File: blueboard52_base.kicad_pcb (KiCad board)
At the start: 2 copper layers, 42.4 x 43.1 mm, 16 parts, among them J1 Conn_East, J2 Conn_West, J3 Conn_South, J4 Conn_VCC, J5 Conn_GND, J6 PBAT, J7 PEXT, SW1 RST, SW2 DFU, U1 E73-2G4M04S-52832

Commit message: Added version info to the board
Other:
- board text added: "v0.1.1, git.io/JegEw"
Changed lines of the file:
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@@
   (general
     (thickness 1.6)
-    (drawings 37)
+    (drawings 38)
     (tracks 172)
     (zones 0)
@@
       (xy -2.020742 1.935137) (xy -2.615037 2.435648) (xy -2.618079 2.434865)) (layer F.SilkS) (width 0))
   )
+  (gr_text "v0.1.1, git.io/JegEw" (at 120.1 89.5) (layer B.SilkS)
+    (effects (font (size 1.5 1.5) (thickness 0.3)) (justify left mirror))
+  )
   (gr_text 15 (at 115.076014 85.275774 270) (layer B.SilkS)

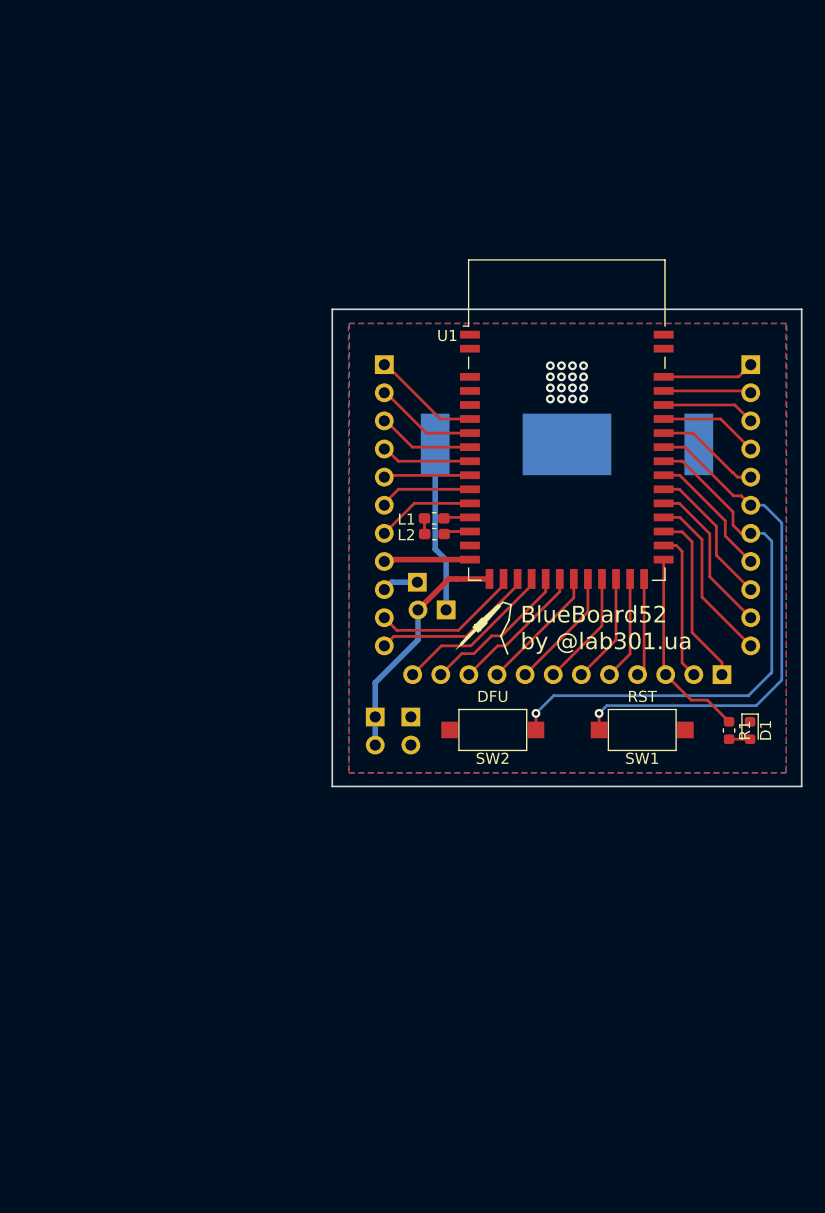
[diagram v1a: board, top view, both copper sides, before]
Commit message: New version of the board - v0.2.0
- Added a separate NFC header
- Created a solid (almost) ground plane on the bottom
- Added silkscreen markings to the top layer
- Removed a bulky power source selector - either a BAT jumper or
  external power source can now be used to power the board
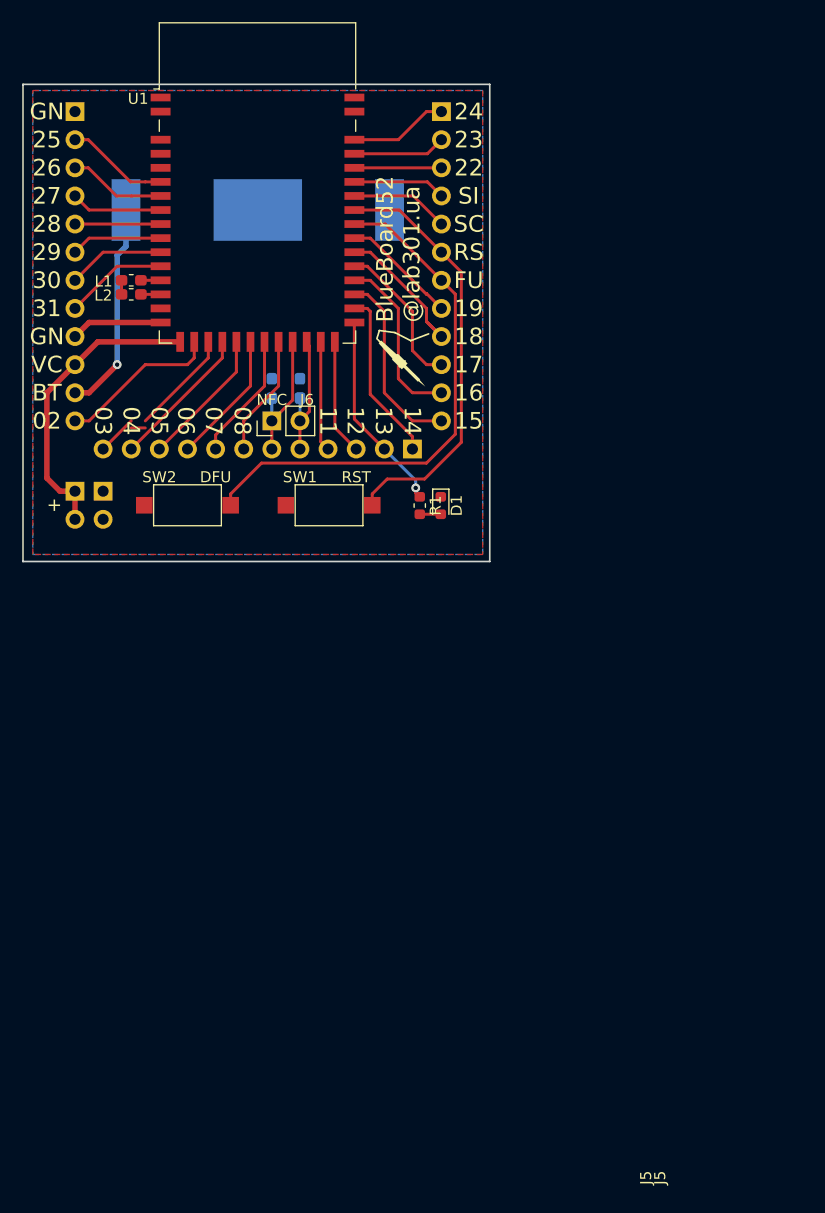
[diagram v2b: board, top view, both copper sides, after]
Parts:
- removed J7: PEXT, Connector_PinHeader_2.54mm:PinHeader_1x01_P2.54mm_Vertical
- added ?: , , F.Cu at (55.4, 62.0)
- added ?: , , F.Cu at (54.1, 62.0)
- added C1: 300pf, Capacitor_SMD:C_0603_1608Metric_Pad1.05x0.95mm_HandSolder, B.Cu at (77.0, 56.5)
- added C2: 300pf, Capacitor_SMD:C_0603_1608Metric_Pad1.05x0.95mm_HandSolder, B.Cu at (74.4, 56.5)
- J1, J2: footprint Connector_PinHeader_2.54mm:PinHeader_1x11_P2.54mm_Vertical -> Connector_PinHeader_2.54mm:PinHeader_1x12_P2.54mm_Vertical
- J4: value Conn_VCC -> VCC
- J5: value Conn_GND -> GND
- J6: value PBAT -> NFC; moved to F.Cu
- moved J1 36.1 mm to (89.8, 31.5)
- moved J2 36.1 mm to (56.7, 31.5)
- moved U1 35.2 mm to (73.1, 38.0)
- moved BT1 35.0 mm to (73.2, 40.4)
- moved L2 34.9 mm to (61.7, 48.0)
- moved SW1 34.8 mm to (79.6, 67.1), turned to 0 degrees
- moved L1 34.8 mm to (61.7, 46.8)
- moved J3 34.6 mm to (87.1, 62.0)
- moved D1 34.5 mm to (89.7, 67.1)
- moved R1 34.5 mm to (87.8, 67.1)
- moved J5 34.5 mm to (59.2, 65.8)
- moved SW2 34.2 mm to (66.8, 67.1)
- moved J4 33.9 mm to (56.7, 65.8)
- moved svg2mod 25.2 mm to (85.9, 53.8), turned to 90 degrees
- moved J6 23.2 mm to (74.4, 59.5)
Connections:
- J2 pad 1: /P0.25 -> GND
- J2 pad 10: /P0.2 -> VCC
- J2 pad 11: /P0.3 -> +BATT
- J2 pad 2: /P0.26 -> /P0.25
- J2 pad 3: /P0.27 -> /P0.26
- J2 pad 4: /P0.28 -> /P0.27
- J2 pad 5: /P0.29 -> /P0.28
- J2 pad 6: /P0.30 -> /P0.29
- J2 pad 7: /P0.31 -> /P0.30
- J2 pad 8: GND -> /P0.31
- J2 pad 9: /EXT_VCC -> GND
- J3 pad 1: /P0.15 -> /P0.14
- J3 pad 10: /P0.6 -> /P0.5
- J3 pad 11: /P0.5 -> /P0.4
- J3 pad 12: /P0.4 -> /P0.3
- J3 pad 2: /P0.14 -> /USER_LED1
- J3 pad 3: /USER_LED1 -> /P0.12
- J3 pad 4: /P0.12 -> /P0.11
- J3 pad 5: /P0.11 -> /P0.10
- J3 pad 6: /P0.10 -> /P0.9
- J3 pad 7: /P0.9 -> /P0.8
- J3 pad 8: /P0.8 -> /P0.7
- J3 pad 9: /P0.7 -> /P0.6
- J6 pad 1: +BATT -> /P0.9
- J6 pad 2: VCC -> /P0.10
- U1 pad 14: Net-(U1-Pad14) -> (no net)
- U1 pad 3: Net-(U1-Pad3) -> (no net)
- U1 pad 4: Net-(U1-Pad4) -> (no net)
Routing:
- net /nRST: track 46.7 -> 38.4 mm, vias 1 -> 0
- net VCC: track 21.4 -> 27.2 mm
- net +BATT: track 15.4 -> 19.2 mm, vias 0 -> 1
- net /EXT_VCC: track 3.26 -> 0.00 mm
- net /P0.10: track 9.94 -> 12.2 mm
- net /P0.14: track 13.5 -> 15.6 mm
- net /P0.9: track 10.5 -> 12.5 mm
- net /P0.2: track 13.5 -> 15.3 mm
- net /P0.12: track 8.88 -> 10.5 mm
- net /P0.4: track 14.7 -> 13.1 mm
- net /DFU: track 49.4 -> 47.9 mm, vias 1 -> 0
- net /P0.18: track 12.9 -> 14.2 mm
- net /P0.5: track 13.7 -> 12.6 mm
- net Net-(L2-Pad2): track 2.89 -> 1.78 mm
- net /P0.19: track 11.6 -> 10.6 mm
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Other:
- board size 42.4 x 43.1 mm -> 42.2 x 43.1 mm
- net class Default: clearance 0.2 -> 0.27; trace_width 0.25 -> 0.27
- net class Power: clearance 0.2 -> 0.27
- rule trace_clearance: 0.2 -> 0.27
- board text added: "+"
- board text added: "04"
- board text added: "05"
- board text added: "BT"
- board text added: "BlueBoard52 @lab301.ua"
- board text added: "v0.2.0 git.io/JvDs8"
- board text removed: "09"
- board text removed: "10"
- board text removed: "BlueBoard52 by @lab301.ua"
- board text removed: "v0.1.1, git.io/JegEw"

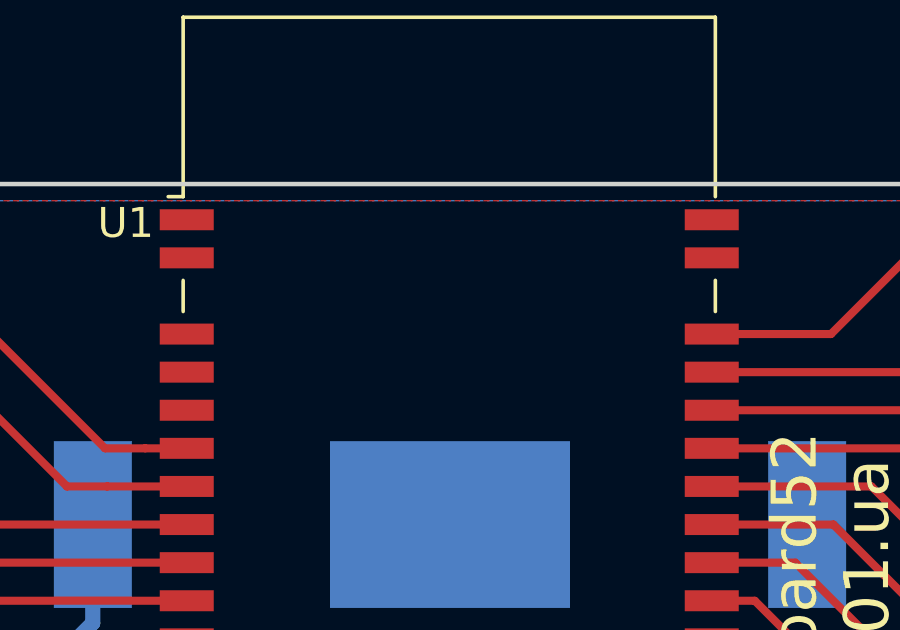
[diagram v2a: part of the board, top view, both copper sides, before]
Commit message: Small fixes - v0.2.1
- Restored a grid of vias between ground planes
- Updated version info in schematic
- Other small fixes
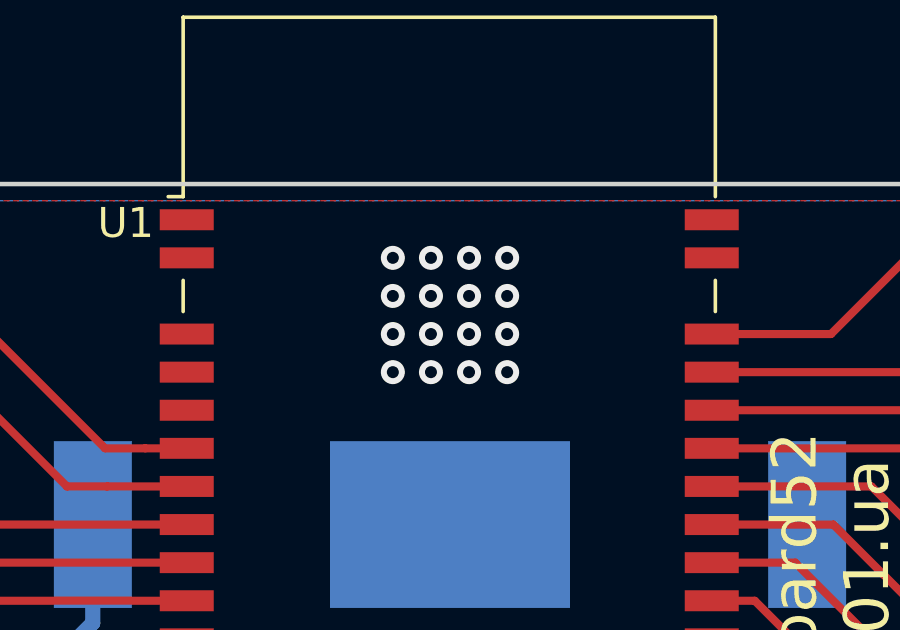
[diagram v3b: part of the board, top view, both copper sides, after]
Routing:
- net GND: vias 0 -> 16
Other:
- board text added: "v0.2.1 git.io/JvDsQ"
- board text removed: "v0.2.0 git.io/JvDs8"
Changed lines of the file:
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@@
     (thickness 1.6)
     (drawings 74)
-    (tracks 138)
+    (tracks 154)
     (zones 0)
     (modules 19)
@@
   (page A4)
   (layers
-    (0 F.Cu signal)
-    (31 B.Cu signal)
+    (0 F.Cu signal hide)
+    (31 B.Cu signal hide)
     (32 B.Adhes user)
     (33 F.Adhes user)
@@
     (add_net "Net-(L1-Pad2)")
     (add_net "Net-(L2-Pad2)")
-    (add_net "Net-(U1-Pad14)")
-    (add_net "Net-(U1-Pad3)")
-    (add_net "Net-(U1-Pad4)")
   )
   (net_class Power ""
@@
     (effects (font (size 1.5 1.5) (thickness 0.3)))
   )
-  (gr_text "v0.2.0 git.io/JvDs8" (at 92.16 69.18) (layer B.SilkS)
+  (gr_text "v0.2.1 git.io/JvDsQ" (at 85.235 67.1) (layer B.SilkS)
     (effects (font (size 1.5 1.5) (thickness 0.3)) (justify left mirror))
   )
@@
   (gr_line (start 94.125 29.08) (end 51.96 29.08) (layer Edge.Cuts) (width 0.15))
   (gr_line (start 94.125 72.18) (end 94.125 29.08) (layer Edge.Cuts) (width 0.15))
+  (via (at 75.075 35.35) (size 0.8) (drill 0.4) (layers F.Cu B.Cu) (net 5))
+  (via (at 75.075 34.08) (size 0.8) (drill 0.4) (layers F.Cu B.Cu) (net 5))
+  (via (at 73.805 35.35) (size 0.8) (drill 0.4) (layers F.Cu B.Cu) (net 5))
+  (via (at 73.805 34.08) (size 0.8) (drill 0.4) (layers F.Cu B.Cu) (net 5))
+  (via (at 72.535 35.35) (size 0.8) (drill 0.4) (layers F.Cu B.Cu) (net 5))
+  (via (at 71.265 35.35) (size 0.8) (drill 0.4) (layers F.Cu B.Cu) (net 5))
+  (via (at 72.535 34.08) (size 0.8) (drill 0.4) (layers F.Cu B.Cu) (net 5))
+  (via (at 71.265 34.08) (size 0.8) (drill 0.4) (layers F.Cu B.Cu) (net 5))
   (segment (start 64.395 46.78) (end 62.615 46.78) (width 0.27) (layer F.Cu) (net 1))
   (segment (start 62.615 48.05) (end 64.395 48.05) (width 0.27) (layer F.Cu) (net 2))
@@
   (segment (start 54.12 56.94) (end 54.12 64.64) (width 0.5) (layer F.Cu) (net 3))
   (segment (start 60.865 46.78) (end 60.865 48.05) (width 0.27) (layer F.Cu) (net 4))
+  (segment (start 57.93 50.59) (end 56.66 51.86) (width 0.5) (layer F.Cu) (net 5))
+  (segment (start 64.395 50.59) (end 57.93 50.59) (width 0.5) (layer F.Cu) (net 5))
+  (via (at 71.265 31.54) (size 0.8) (drill 0.4) (layers F.Cu B.Cu) (net 5))
+  (via (at 72.535 31.54) (size 0.8) (drill 0.4) (layers F.Cu B.Cu) (net 5))
+  (via (at 73.805 31.54) (size 0.8) (drill 0.4) (layers F.Cu B.Cu) (net 5))
+  (via (at 75.075 31.54) (size 0.8) (drill 0.4) (layers F.Cu B.Cu) (net 5))
+  (via (at 75.075 32.81) (size 0.8) (drill 0.4) (layers F.Cu B.Cu) (net 5))
+  (via (at 73.805 32.81) (size 0.8) (drill 0.4) (layers F.Cu B.Cu) (net 5))
+  (via (at 72.535 32.81) (size 0.8) (drill 0.4) (layers F.Cu B.Cu) (net 5))
+  (via (at 71.265 32.81) (size 0.8) (drill 0.4) (layers F.Cu B.Cu) (net 5))
   (segment (start 84.68 41.7) (end 89.76 46.78) (width 0.27) (layer F.Cu) (net 6))
   (segment (start 81.895 41.7) (end 84.68 41.7) (width 0.27) (layer F.Cu) (net 6))
   (segment (start 89.76 46.78) (end 91.015001 48.035001) (width 0.27) (layer F.Cu) (net 6))
+  (segment (start 73.51 63.29) (end 70.72 66.08) (width 0.27) (layer F.Cu) (net 6))
+  (segment (start 91.015001 48.035001) (end 91.015001 60.684999) (width 0.27) (layer F.Cu) (net 6))
+  (segment (start 70.72 66.08) (end 70.72 67.1) (width 0.27) (layer F.Cu) (net 6))
+  (segment (start 88.41 63.29) (end 73.51 63.29) (width 0.27) (layer F.Cu) (net 6))
+  (segment (start 91.015001 60.684999) (end 88.41 63.29) (width 0.27) (layer F.Cu) (net 6))
   (segment (start 89.701837 67.913267) (end 87.801837 67.913267) (width 0.27) (layer F.Cu) (net 7))
   (via (at 87.435535 65.534465) (size 0.8) (drill 0.4) (layers F.Cu B.Cu) (net 8))
@@
   (segment (start 81.895 50.59) (end 81.895 59.315) (width 0.27) (layer F.Cu) (net 8))
   (segment (start 87.435535 65.971965) (end 87.801837 66.338267) (width 0.27) (layer F.Cu) (net 8))
+  (segment (start 87.435535 65.534465) (end 87.435535 65.971965) (width 0.27) (layer F.Cu) (net 8))
+  (segment (start 87.435535 64.855535) (end 87.435535 65.534465) (width 0.27) (layer B.Cu) (net 8))
+  (segment (start 84.6 62.02) (end 87.435535 64.855535) (width 0.27) (layer B.Cu) (net 8))
   (segment (start 85.95 40.43) (end 89.76 44.24) (width 0.27) (layer F.Cu) (net 9))
   (segment (start 81.895 40.43) (end 85.95 40.43) (width 0.27) (layer F.Cu) (net 9))
   (segment (start 89.76 44.24) (end 91.555011 46.035011) (width 0.27) (layer F.Cu) (net 9))
+  (segment (start 91.555011 46.035011) (end 91.555011 61.414989) (width 0.27) (layer F.Cu) (net 9))
+  (segment (start 83.51 66.08) (end 83.51 67.1) (width 0.27) (layer F.Cu) (net 9))
+  (segment (start 84.860536 64.729464) (end 83.51 66.08) (width 0.27) (layer F.Cu) (net 9))
+  (segment (start 88.240536 64.729464) (end 84.860536 64.729464) (width 0.27) (layer F.Cu) (net 9))
+  (segment (start 91.555011 61.414989) (end 88.240536 64.729464) (width 0.27) (layer F.Cu) (net 9))
   (segment (start 87.22 39.16) (end 89.76 41.7) (width 0.27) (layer F.Cu) (net 10))
   (segment (start 81.895 39.16) (end 87.22 39.16) (width 0.27) (layer F.Cu) (net 10))
@@
   (segment (start 63.01 60.115) (end 61.74 60.115) (width 0.27) (layer F.Cu) (net 12))
   (segment (start 67.43 52.34) (end 67.43 53.049002) (width 0.27) (layer F.Cu) (net 13))
-  (segment (start 57.93 50.59) (end 56.66 51.86) (width 0.5) (layer F.Cu) (net 5))
-  (segment (start 64.395 50.59) (end 57.93 50.59) (width 0.5) (layer F.Cu) (net 5))
-  (segment (start 73.51 63.29) (end 70.72 66.08) (width 0.27) (layer F.Cu) (net 6))
-  (segment (start 91.015001 48.035001) (end 91.015001 60.684999) (width 0.27) (layer F.Cu) (net 6))
-  (segment (start 70.72 66.08) (end 70.72 67.1) (width 0.27) (layer F.Cu) (net 6))
-  (segment (start 88.41 63.29) (end 73.51 63.29) (width 0.27) (layer F.Cu) (net 6))
-  (segment (start 91.015001 60.684999) (end 88.41 63.29) (width 0.27) (layer F.Cu) (net 6))
-  (segment (start 87.435535 65.534465) (end 87.435535 65.971965) (width 0.27) (layer F.Cu) (net 8))
-  (segment (start 87.435535 64.855535) (end 87.435535 65.534465) (width 0.27) (layer B.Cu) (net 8))
-  (segment (start 84.6 62.02) (end 87.435535 64.855535) (width 0.27) (layer B.Cu) (net 8))
-  (segment (start 91.555011 46.035011) (end 91.555011 61.414989) (width 0.27) (layer F.Cu) (net 9))
-  (segment (start 83.51 66.08) (end 83.51 67.1) (width 0.27) (layer F.Cu) (net 9))
-  (segment (start 84.860536 64.729464) (end 83.51 66.08) (width 0.27) (layer F.Cu) (net 9))
-  (segment (start 88.240536 64.729464) (end 84.860536 64.729464) (width 0.27) (layer F.Cu) (net 9))
-  (segment (start 91.555011 61.414989) (end 88.240536 64.729464) (width 0.27) (layer F.Cu) (net 9))
   (segment (start 67.43 52.34) (end 67.43 53.79) (width 0.27) (layer F.Cu) (net 13))
   (segment (start 67.43 53.79) (end 66.82 54.4) (width 0.27) (layer F.Cu) (net 13))
@@
   (segment (start 61.265 43.71) (end 60.47 44.505) (width 0.5) (layer B.Cu) (net 14))
   (segment (start 61.265 40.43) (end 61.265 43.71) (width 0.5) (layer B.Cu) (net 14))
-  (via (at 60.47 54.4) (size 0.8) (drill 0.4) (layers F.Cu B.Cu) (net 14) (status 1000000))
+  (via (at 60.47 54.4) (size 0.8) (drill 0.4) (layers F.Cu B.Cu) (net 14))
   (segment (start 57.93 56.94) (end 60.47 54.4) (width 0.5) (layer F.Cu) (net 14))
   (segment (start 56.66 56.94) (end 57.93 56.94) (width 0.5) (layer F.Cu) (net 14))
